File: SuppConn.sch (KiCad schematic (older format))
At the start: 7 parts, among them J5 SuppPowerConnector, U7 OPAx192-Q1, U9 OPA388-Q1

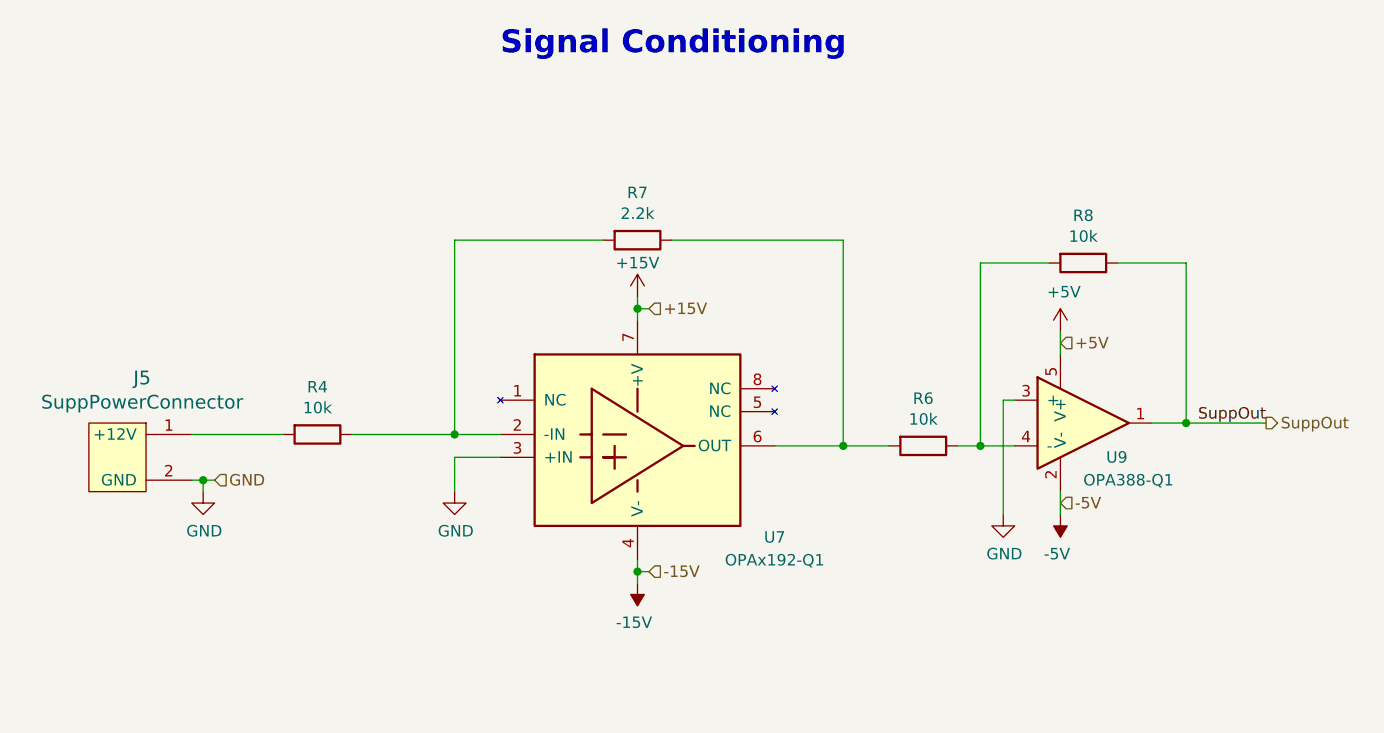
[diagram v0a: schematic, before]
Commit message: Edits opamp circuitry to just one opamp and adds keepout zone under 12V and GNDPWR
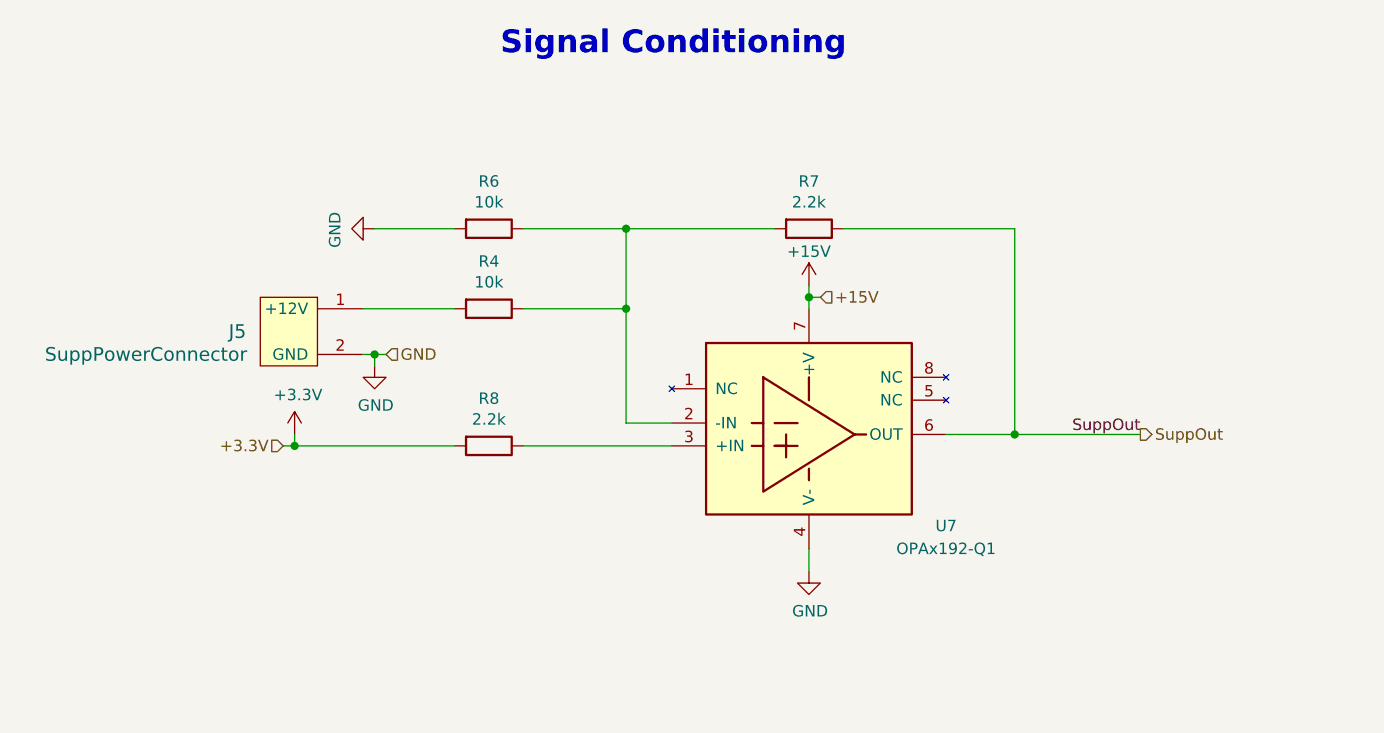
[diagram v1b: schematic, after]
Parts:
- removed U9: OPA388-Q1, Package_TO_SOT_SMD:SOT-23-5, symbol utsvt-chips:OPA388-Q1
- R8: value 10k -> 2.2k
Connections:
- net -15V is gone; now on net GND: U7.4 (V-)
- net GND: now also R6.2; no longer U7.3 (+IN)
- net SuppOut: now also R7.1, U7.6 (OUT); no longer R8.1
- net at R4.1, R7.2, U7.2 (-IN): now also R6.1
- net +3V3: now reaches R8.2
- net +3V3: no longer R6.1
- new net: R8.1, U7.3 (+IN)
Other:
- moved on the sheet: J5, R4, R7, U7

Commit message: Correct op amp voltage measurement circuitry
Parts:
- added R9: 24k, Resistor_SMD:R_0805_2012Metric, symbol Device:R
- R8: value 2.2k -> 11k
- U7: symbol utsvt-chips:OPAx192-Q1 -> Power-SupplementalMonitoringPCB-rescue:OPAx192-Q1-utsvt-chips
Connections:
- net GND: now also R9.1
- net at R8.1, U7.3 (+IN): now also R9.2
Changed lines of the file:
@@
 Signal Conditioning
 $Comp
-L utsvt-chips:OPAx192-Q1 U7
+L Power-SupplementalMonitoringPCB-rescue:OPAx192-Q1-utsvt-chips U7
 U 1 1 5FF22F96
 P 6500 5200
+AR Path="/5FF22F96" Ref="U7"  Part="1"
+AR Path="/5FD73B7C/5FF22F96" Ref="U7"  Part="1"
 F 0 "U7" H 7100 5800 50  0000 C CNN
 F 1 "OPAx192-Q1" H 7100 5700 50  0000 C CNN
@@
 Wire Wire Line
 	5700 3650 5700 4150
-$Comp
-L Device:R R8
-U 1 1 5FE0625E
-P 5100 4250
-F 0 "R8" V 4893 4250 50  0000 C CNN
-F 1 "2.2k" V 4984 4250 50  0000 C CNN
-F 2 "Resistor_SMD:R_0805_2012Metric" V 5030 4250 50  0001 C CNN
-F 3 "~" H 5100 4250 50  0001 C CNN
-	1    5100 4250
-	0    1    1    0
-$EndComp
-Wire Wire Line
-	5250 4250 5900 4250
-Wire Wire Line
-	4950 4250 4250 4250
 Wire Wire Line
 	4250 4250 4250 4200
@@
 Wire Wire Line
 	4250 4250 4200 4250
+$Comp
+L Device:R R8
+U 1 1 5FDF6EAC
+P 4350 4400
+F 0 "R8" V 4143 4400 50  0000 C CNN
+F 1 "11k" V 4234 4400 50  0000 C CNN
+F 2 "Resistor_SMD:R_0805_2012Metric" V 4280 4400 50  0001 C CNN
+F 3 "~" H 4350 4400 50  0001 C CNN
+	1    4350 4400
+	-1   0    0    1
+$EndComp
+$Comp
+L Device:R R9
+U 1 1 5FDF759A
+P 4350 4950
+F 0 "R9" V 4143 4950 50  0000 C CNN
+F 1 "24k" V 4234 4950 50  0000 C CNN
+F 2 "Resistor_SMD:R_0805_2012Metric" V 4280 4950 50  0001 C CNN
+F 3 "~" H 4350 4950 50  0001 C CNN
+	1    4350 4950
+	-1   0    0    1
+$EndComp
+$Comp
+L power:GND #PWR05
+U 1 1 5FDF799E
+P 4350 5200
+F 0 "#PWR05" H 4350 4950 50  0001 C CNN
+F 1 "GND" H 4355 5027 50  0000 C CNN
+F 2 "" H 4350 5200 50  0001 C CNN
+F 3 "" H 4350 5200 50  0001 C CNN
+	1    4350 5200
+	1    0    0    -1
+$EndComp
+Wire Wire Line
+	4350 5200 4350 5100
+Wire Wire Line
+	4350 4800 4350 4650
+Wire Wire Line
+	4350 4250 4250 4250
 Connection ~ 4250 4250
+Wire Wire Line
+	4350 4650 5150 4650
+Wire Wire Line
+	5150 4650 5150 4250
+Wire Wire Line
+	5150 4250 5900 4250
+Connection ~ 4350 4650
+Wire Wire Line
+	4350 4650 4350 4550
 $EndSCHEMATC

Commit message: Fixes opamp circuitry
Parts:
- U7: symbol Power-SupplementalMonitoringPCB-rescue:OPAx192-Q1-utsvt-chips -> utsvt-chips:OPAx192-Q1
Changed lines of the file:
@@
 Signal Conditioning
 $Comp
-L Power-SupplementalMonitoringPCB-rescue:OPAx192-Q1-utsvt-chips U7
+L utsvt-chips:OPAx192-Q1 U7
 U 1 1 5FF22F96
 P 6500 5200
